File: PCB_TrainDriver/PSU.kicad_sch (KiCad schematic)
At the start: 20 parts, among them U8 TPSM863257RDXR, U9 LDL1117S33R

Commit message: Finished sch
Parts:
- removed C28: 220uF, Capacitor_SMD:CP_Elec_6.3x5.4, symbol Device:C_Polarized_Small
- removed R21: 28.7k, Resistor_SMD:R_0402_1005Metric, symbol Device:R_Small
- removed R22: 10k, Resistor_SMD:R_0402_1005Metric, symbol Device:R_Small
- removed U8: TPSM863257RDXR, SamacSys_Parts:QFN-7_L4.0-W3.3_TPSM863257RDXR, symbol SamacSys_Parts:TPSM863257RDXR
- added C28, C32: 0.1uF 50V, Capacitor_SMD:C_0402_1005Metric, symbol Device:C_Small
- added C31: 1uF, Capacitor_SMD:C_0402_1005Metric, symbol Device:C_Small
- added CN1: XT90PW-M.G.Y, Sharing_Footprint:CONN-TH_XT90PW-M.G.Y, symbol Sharing_Symbol:XT90PW-M.G.Y
- added L1: 10uH 21mOhms, Inductor_SMD:L_12x12mm_H4.5mm, symbol Device:L
- added R18: 0.25mOhms 15W, Sharing_Footprint:R5930, symbol Device:R
- added R25, R26: 4.7k, Resistor_SMD:R_0402_1005Metric, symbol Device:R_Small
- added U4: TPS62932, Package_TO_SOT_SMD:SOT-583-8, symbol Regulator_Switching:TPS62932
- added U6: INA219AxDCN, Package_TO_SOT_SMD:SOT-23-8, symbol Sensor_Energy:INA219AxDCN
- C20: value 10uF -> 10uF 50V; footprint Capacitor_SMD:C_0402_1005Metric -> Capacitor_SMD:C_1206_3216Metric; JLCPCB Part # (none) -> C13585; LCSC Part # C77000 -> (none); Package (none) -> 1210
- C21: value 0.1uF -> 0.1uF 50V; footprint Capacitor_SMD:C_0402_1005Metric -> Capacitor_SMD:C_0603_1608Metric; JLCPCB Part # (none) -> C14663; LCSC Part # C71687 -> (none); Package (none) -> 0603
- C22: value 10nF -> 33nF 10V; JLCPCB Part # (none) -> C527022; LCSC Part # C541371 -> (none); Package (none) -> 0402
- C23: value 22pF -> 18pF 25V; JLCPCB Part # (none) -> C526984; LCSC Part # C1555 -> (none); Package (none) -> 0402
- C24: value 33uF -> 47uF 16V; footprint Capacitor_SMD:C_0402_1005Metric -> Capacitor_SMD:C_1206_3216Metric; JLCPCB Part # (none) -> C7472975; LCSC Part # C1160 -> (none); Package (none) -> 1206
- C25: value 0.1uF -> 0.1uF 50V; JLCPCB Part # (none) -> C307331; LCSC Part # C71687 -> (none); LCSC Part# C1525 -> (none); Package (none) -> 0402
- C26: JLCPCB Part # (none) -> C52923; LCSC Part # C14445 -> (none); LCSC Part# C29266 -> (none); Package (none) -> 0402
- C27: JLCPCB Part # (none) -> C412252; LCSC Part # C412252 -> (none); LCSC Part# C412252 -> (none); Package (none) -> 1206
- D6: footprint LED_SMD:LED_0402_1005Metric -> LED_SMD:LED_0603_1608Metric; JLCPCB Part # (none) -> C2286; LCSC Part # C71911 -> (none)
- R23: value 220k -> 52.3k; footprint Resistor_SMD:R_0402_1005Metric -> Resistor_SMD:R_0603_1608Metric; JLCPCB Part # (none) -> C23198; LCSC Part # C25767 -> (none); Package (none) -> 0603
- R24: value 30k -> 10k; JLCPCB Part # (none) -> C25744; LCSC Part # C25553 -> (none); Package (none) -> 0402
- R38: JLCPCB Part # (none) -> C11702; LCSC Part # C106235 -> (none); Package (none) -> 0402
- TP1: value BATT+ -> VCC
- U9: JLCPCB Part # (none) -> C18906017; LCSC Part # C435835 -> (none); LCSC Part# C435835 -> (none)
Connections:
- net +3.3V: now also C32.2, R25.1, R26.1, U6.4 (VS)
- net +5V: now also C31.1, L1.2
- net GND: now also C31.2, C32.1, CN1.1, U4.4 (GND), U6.3 (GND), U6.7 (A0), U6.8 (A1)
- net VCC: now also CN1.2, R18.1, U6.1 (IN+); no longer C20.2, C21.2, TP1.1
- net at C22.2: now also U4.7 (SS)
- net at C23.1, R23.1, R24.2: now also U4.8 (FB)
- new net: C28.2, L1.1, U4.5 (SW)
- new net: C28.1, U4.6 (BST)
- new net +12V: C20.2, C21.2, R18.2, TP1.1, U4.3 (VIN), U6.2 (IN-)
- new net INA219_SCL: R26.2, U6.5 (SCL)
- new net INA219_SDA: R25.2, U6.6 (SDA)
- no-connect marks 2 -> 4
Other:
- moved on the sheet: C22, C23, C24, R23, R24, TP2

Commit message: PCB Almost Finished
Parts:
- removed R38: 1k, Resistor_SMD:R_0402_1005Metric, symbol Device:R_Small
- added R27: 1k, Resistor_SMD:R_0402_1005Metric, symbol Device:R_Small
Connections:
- net +3.3V: now also R27.1
- net at D6.2 (A): now also R27.2
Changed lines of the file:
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@@
-	)
-	(symbol
-		(lib_id "Device:R_Small")
-		(at 218.44 142.24 270)
-		(mirror x)
-		(unit 1)
-		(body_style 1)
-		(exclude_from_sim no)
-		(in_bom yes)
-		(on_board no)
-		(in_pos_files yes)
-		(dnp no)
-		(property "Reference" "R38"
-			(at 218.44 140.462 90)
-			(show_name no)
-			(do_not_autoplace no)
-			(effects
-				(font
-					(size 1.016 1.016)
-				)
-			)
-		)
-		(property "Value" "1k"
-			(at 218.421 142.2933 90)
-			(show_name no)
-			(do_not_autoplace no)
-			(effects
-				(font
-					(size 0.762 0.762)
-				)
-			)
-		)
-		(property "Footprint" "Resistor_SMD:R_0402_1005Metric"
-			(at 218.44 142.24 0)
-			(hide yes)
-			(show_name no)
-			(do_not_autoplace no)
-			(effects
-				(font
-					(size 1.27 1.27)
-				)
-			)
-		)
-		(property "Datasheet" ""
-			(at 218.44 142.24 0)
-			(hide yes)
-			(show_name no)
-			(do_not_autoplace no)
-			(effects
-				(font
-					(size 1.27 1.27)
-				)
-			)
-		)
-		(property "Description" "Resistor, small symbol"
-			(at 218.44 142.24 0)
-			(hide yes)
-			(show_name no)
-			(do_not_autoplace no)
-			(effects
-				(font
-					(size 1.27 1.27)
-				)
-			)
-		)
-		(property "JLCPCB Part #" "C11702"
-			(at 218.44 142.24 90)
-			(hide yes)
-			(show_name no)
-			(do_not_autoplace no)
-			(effects
-				(font
-					(size 1.27 1.27)
-				)
-			)
-		)
-		(property "Package" "0402"
-			(at 218.44 144.272 90)
-			(show_name no)
-			(do_not_autoplace no)
-			(effects
-				(font
-					(size 1.27 1.27)
-				)
-			)
-		)
-		(property "LCSC Part #" ""
-			(at 218.44 142.24 90)
-			(hide yes)
-			(show_name no)
-			(do_not_autoplace no)
-			(effects
-				(font
-					(size 1.27 1.27)
-				)
-			)
-		)
-		(property "LCSC Part#" ""
-			(at 218.44 142.24 90)
-			(hide yes)
-			(show_name no)
-			(do_not_autoplace no)
-			(effects
-				(font
-					(size 1.27 1.27)
-				)
-			)
-		)
-		(pin "1"
-		)
-		(pin "2"
-		)
-		(instances
-			(project "PCB_TrainDriver"
-				(path "/f74253cb-ef08-441b-b3c3-36bc664bf8d8/4e4ac9ff-7b76-4f1d-9093-ce2b1ba9f40d"
-					(reference "R38")
-					(unit 1)
-				)
-			)
-		)
 	)
 	(symbol
@@
 					(unit 1)
 				)
+			)
+		)
+	)
+	(symbol
+		(lib_id "Device:R_Small")
+		(at 218.44 142.24 90)
+		(unit 1)
+		(body_style 1)
+		(exclude_from_sim no)
+		(in_bom yes)
+		(on_board yes)
+		(in_pos_files yes)
+		(dnp no)
+		(property "Reference" "R27"
+			(at 218.44 140.208 90)
+			(show_name no)
+			(do_not_autoplace no)
+			(effects
+				(font
+					(size 1.016 1.016)
+				)
+			)
+		)
+		(property "Value" "1k"
+			(at 218.459 142.2933 90)
+			(show_name no)
+			(do_not_autoplace no)
+			(effects
+				(font
+					(size 0.762 0.762)
+				)
+			)
+		)
+		(property "Footprint" "Resistor_SMD:R_0402_1005Metric"
+			(at 218.44 142.24 0)
+			(hide yes)
+			(show_name no)
+			(do_not_autoplace no)
+			(effects
+				(font
+					(size 1.27 1.27)
+				)
+			)
+		)
+		(property "Datasheet" ""
+			(at 218.44 142.24 0)
+			(hide yes)
+			(show_name no)
+			(do_not_autoplace no)
+			(effects
+				(font
+					(size 1.27 1.27)
+				)
+			)
+		)
+		(property "Description" "Resistor, small symbol"
+			(at 218.44 142.24 0)
+			(hide yes)
+			(show_name no)
+			(do_not_autoplace no)
+			(effects
+				(font
+					(size 1.27 1.27)
+				)
+			)
+		)
+		(property "JLCPCB Part #" "C25900"
+			(at 218.44 142.24 0)
+			(hide yes)
+			(show_name no)
+			(do_not_autoplace no)
+			(effects
+				(font
+					(size 1.27 1.27)
+				)
+			)
+		)
+		(property "Package" "0402"
+			(at 218.44 144.272 90)
+			(show_name no)
+			(do_not_autoplace no)
+			(effects
+				(font
+					(size 1.27 1.27)
+				)
+			)
+		)
+		(property "LCSC Part #" ""
+			(at 218.44 142.24 90)
+			(hide yes)
+			(show_name no)
+			(do_not_autoplace no)
+			(effects
+				(font
+					(size 1.27 1.27)
+				)
+			)
+		)
+		(property "LCSC Part#" ""
+			(at 218.44 142.24 90)
+			(hide yes)
+			(show_name no)
+			(do_not_autoplace no)
+			(effects
+				(font
+					(size 1.27 1.27)
+				)
+			)
+		)
+		(pin "1"
+		)
+		(pin "2"
+		)
+		(instances
+			(project "PCB_TrainDriver"
+				(path "/f74253cb-ef08-441b-b3c3-36bc664bf8d8/4e4ac9ff-7b76-4f1d-9093-ce2b1ba9f40d"
+					(reference "R27")
+					(unit 1)
+				)

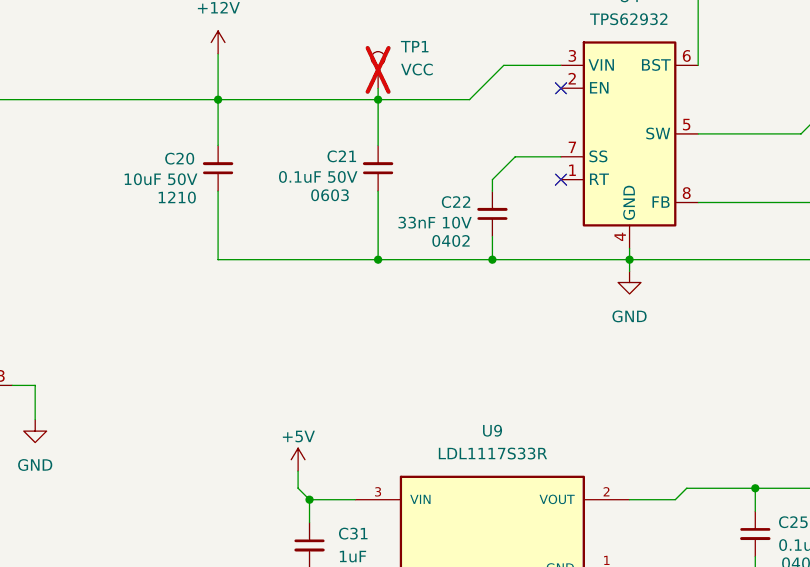
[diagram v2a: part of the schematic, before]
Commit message: Add aux led indicator
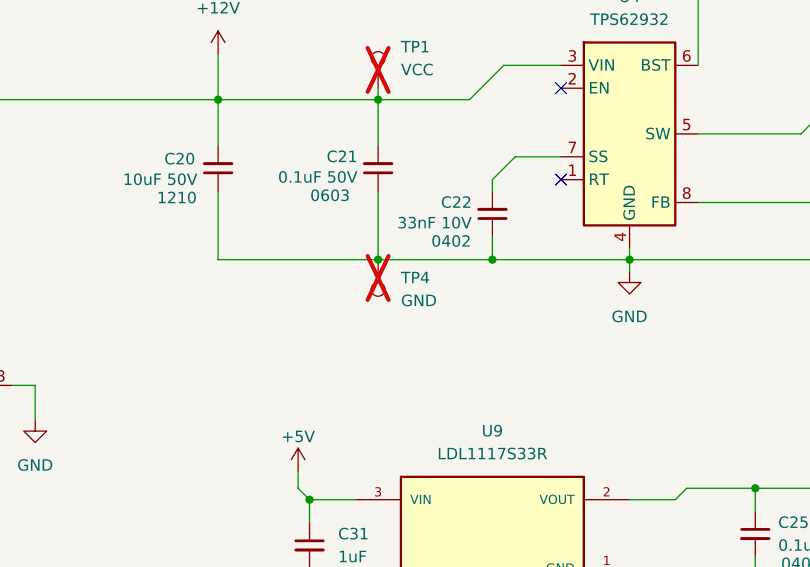
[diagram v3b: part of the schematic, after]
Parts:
- added TP4: GND, Connector_Pin:Pin_D0.7mm_L6.5mm_W1.8mm_FlatFork, symbol Connector:TestPoint
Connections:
- net GND: now also TP4.1
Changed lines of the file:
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@@
+	)
+	(symbol
+		(lib_id "Connector:TestPoint")
+		(at 105.41 111.76 180)
+		(unit 1)
+		(body_style 1)
+		(exclude_from_sim no)
+		(in_bom no)
+		(on_board yes)
+		(in_pos_files yes)
+		(dnp yes)
+		(fields_autoplaced yes)
+		(property "Reference" "TP4"
+			(at 107.95 113.7919 0)
+			(show_name no)
+			(do_not_autoplace no)
+			(effects
+				(font
+					(size 1.27 1.27)
+				)
+				(justify right)
+			)
+		)
+		(property "Value" "GND"
+			(at 107.95 116.3319 0)
+			(show_name no)
+			(do_not_autoplace no)
+			(effects
+				(font
+					(size 1.27 1.27)
+				)
+				(justify right)
+			)
+		)
+		(property "Footprint" "Connector_Pin:Pin_D0.7mm_L6.5mm_W1.8mm_FlatFork"
+			(at 100.33 111.76 0)
+			(hide yes)
+			(show_name no)
+			(do_not_autoplace no)
+			(effects
+				(font
+					(size 1.27 1.27)
+				)
+			)
+		)
+		(property "Datasheet" ""
+			(at 100.33 111.76 0)
+			(hide yes)
+			(show_name no)
+			(do_not_autoplace no)
+			(effects
+				(font
+					(size 1.27 1.27)
+				)
+			)
+		)
+		(property "Description" "test point"
+			(at 105.41 111.76 0)
+			(hide yes)
+			(show_name no)
+			(do_not_autoplace no)
+			(effects
+				(font
+					(size 1.27 1.27)
+				)
+			)
+		)
+		(property "JLCPCB Part #" ""
+			(at 105.41 111.76 0)
+			(hide yes)
+			(show_name no)
+			(do_not_autoplace no)
+			(effects
+				(font
+					(size 1.27 1.27)
+				)
+			)
+		)
+		(property "LCSC Part #" ""
+			(at 105.41 111.76 0)
+			(hide yes)
+			(show_name no)
+			(do_not_autoplace no)
+			(effects
+				(font
+					(size 1.27 1.27)
+				)
+			)
+		)
+		(property "LCSC Part#" ""
+			(at 105.41 111.76 0)
+			(hide yes)
+			(show_name no)
+			(do_not_autoplace no)
+			(effects
+				(font
+					(size 1.27 1.27)
+				)
+			)
+		)
+		(pin "1"
+		)
+		(instances
+			(project "PCB_TrainDriver"
+				(path "/f74253cb-ef08-441b-b3c3-36bc664bf8d8/4e4ac9ff-7b76-4f1d-9093-ce2b1ba9f40d"
+					(reference "TP4")
+					(unit 1)
+				)
+			)
+		)
 	)
 	(symbol
